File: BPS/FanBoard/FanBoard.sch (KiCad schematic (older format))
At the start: 13 parts, among them J1 Conn_01x02, J2 Conn_01x02, J3 Conn_01x02, J4 Conn_01x02, J5 Conn_01x06, Q1 BUK9M34-100EX, Q2 BUK9M34-100EX, Q3 BUK9M34-100EX, Q4 BUK9M34-100EX

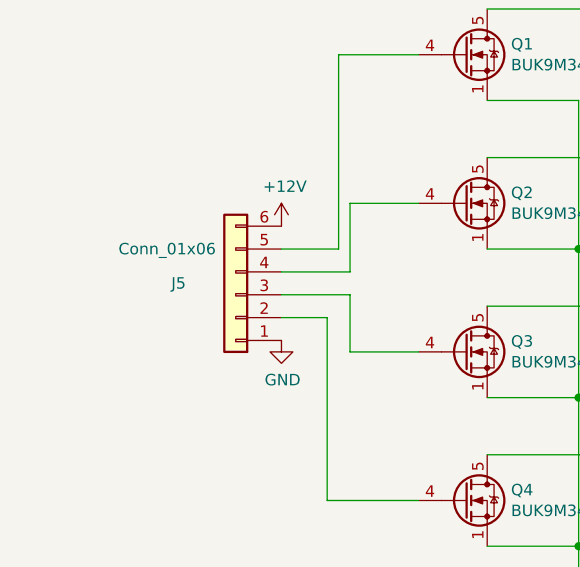
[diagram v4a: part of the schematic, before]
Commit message: Changed Leader board connections and changed footprints of fan connections to molex 3mm
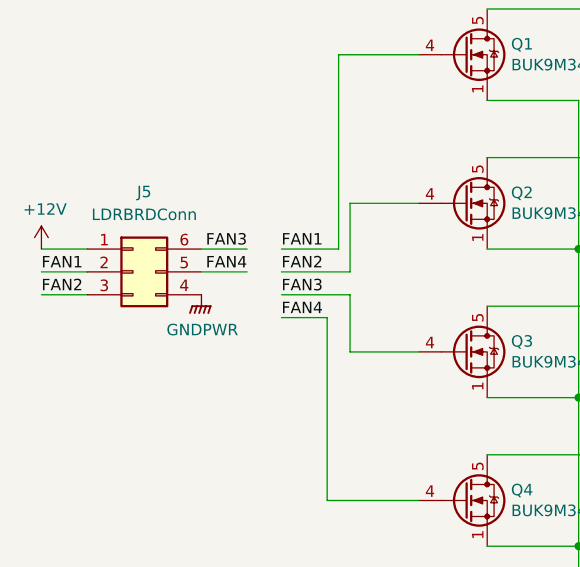
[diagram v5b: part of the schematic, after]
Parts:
- removed J5: Conn_01x06, symbol Connector_Generic:Conn_01x06
- added J5: LDRBRDConn, symbol Connector_Generic:Conn_02x03_Counter_Clockwise
- J1, J2, J3, J4: footprint Connector_PinSocket_2.54mm:PinSocket_1x02_P2.54mm_Vertical -> UTSVT_Connectors:Molex_MicroFit3.0_1x2xP3.00mm_PolarizingPeg_Vertical
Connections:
- net +12V: now also J5.1 (Pin_1)
- net FAN1: now reaches Q1.4 (G)
- net FAN1: now also J5.2 (Pin_2)
- net FAN2: now reaches Q2.4 (G)
- net FAN2: now also J5.3 (Pin_3)
- net FAN3: now reaches Q3.4 (G)
- net FAN3: now also J5.6 (Pin_6)
- net FAN4: now reaches Q4.4 (G)
- net FAN4: now also J5.5 (Pin_5)
- new net GNDPWR: J5.4 (Pin_4)
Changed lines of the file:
@@
 F 0 "J1" H 4330 3642 50  0000 L CNN
 F 1 "Conn_01x02" H 4330 3551 50  0000 L CNN
-F 2 "Connector_PinSocket_2.54mm:PinSocket_1x02_P2.54mm_Vertical" H 4250 3650 50  0001 C CNN
+F 2 "UTSVT_Connectors:Molex_MicroFit3.0_1x2xP3.00mm_PolarizingPeg_Vertical" H 4250 3650 50  0001 C CNN
 F 3 "~" H 4250 3650 50  0001 C CNN
 	1    4250 3650
@@
 F 0 "J2" H 4330 4292 50  0000 L CNN
 F 1 "Conn_01x02" H 4330 4201 50  0000 L CNN
-F 2 "Connector_PinSocket_2.54mm:PinSocket_1x02_P2.54mm_Vertical" H 4250 4300 50  0001 C CNN
+F 2 "UTSVT_Connectors:Molex_MicroFit3.0_1x2xP3.00mm_PolarizingPeg_Vertical" H 4250 4300 50  0001 C CNN
 F 3 "~" H 4250 4300 50  0001 C CNN
 	1    4250 4300
@@
 F 0 "J3" H 4330 4942 50  0000 L CNN
 F 1 "Conn_01x02" H 4330 4851 50  0000 L CNN
-F 2 "Connector_PinSocket_2.54mm:PinSocket_1x02_P2.54mm_Vertical" H 4250 4950 50  0001 C CNN
+F 2 "UTSVT_Connectors:Molex_MicroFit3.0_1x2xP3.00mm_PolarizingPeg_Vertical" H 4250 4950 50  0001 C CNN
 F 3 "~" H 4250 4950 50  0001 C CNN
 	1    4250 4950
@@
 F 0 "J4" H 4330 5592 50  0000 L CNN
 F 1 "Conn_01x02" H 4330 5501 50  0000 L CNN
-F 2 "Connector_PinSocket_2.54mm:PinSocket_1x02_P2.54mm_Vertical" H 4250 5600 50  0001 C CNN
+F 2 "UTSVT_Connectors:Molex_MicroFit3.0_1x2xP3.00mm_PolarizingPeg_Vertical" H 4250 5600 50  0001 C CNN
 F 3 "~" H 4250 5600 50  0001 C CNN
 	1    4250 5600
@@
 	2500 5100 2300 5100
 $Comp
-L Connector_Generic:Conn_01x06 J5
-U 1 1 5F1BB034
-P 2100 5000
-F 0 "J5" H 2350 4950 50  0000 C CNN
-F 1 "Conn_01x06" H 2400 4800 50  0000 C CNN
-F 2 "" H 2100 5000 50  0001 C CNN
-F 3 "~" H 2100 5000 50  0001 C CNN
-	1    2100 5000
-	-1   0    0    1
-$EndComp
-$Comp
 L power:+12V #PWR03
 U 1 1 5F1BC556
-P 2300 4700
-F 0 "#PWR03" H 2300 4550 50  0001 C CNN
-F 1 "+12V" H 2315 4873 50  0000 C CNN
-F 2 "" H 2300 4700 50  0001 C CNN
-F 3 "" H 2300 4700 50  0001 C CNN
-	1    2300 4700
-	1    0    0    -1
-$EndComp
-$Comp
-L power:GND #PWR04
-U 1 1 5F1BCBA1
-P 2300 5200
-F 0 "#PWR04" H 2300 4950 50  0001 C CNN
-F 1 "GND" H 2305 5027 50  0000 C CNN
-F 2 "" H 2300 5200 50  0001 C CNN
-F 3 "" H 2300 5200 50  0001 C CNN
-	1    2300 5200
-	1    0    0    -1
-$EndComp
+P 1250 4800
+F 0 "#PWR03" H 1250 4650 50  0001 C CNN
+F 1 "+12V" H 1265 4973 50  0000 C CNN
+F 2 "" H 1250 4800 50  0001 C CNN
+F 3 "" H 1250 4800 50  0001 C CNN
+	1    1250 4800
+	1    0    0    -1
+$EndComp
+$Comp
+L Connector_Generic:Conn_02x03_Counter_Clockwise J5
+U 1 1 5F1BA642
+P 1650 4900
+F 0 "J5" H 1700 5250 50  0000 C CNN
+F 1 "LDRBRDConn" H 1700 5150 50  0000 C CNN
+F 2 "" H 1650 4900 50  0001 C CNN
+F 3 "~" H 1650 4900 50  0001 C CNN
+	1    1650 4900
+	1    0    0    -1
+$EndComp
+$Comp
+L power:GNDPWR #PWR04
+U 1 1 5F1BB28B
+P 1950 5000
+F 0 "#PWR04" H 1950 4800 50  0001 C CNN
+F 1 "GNDPWR" H 1954 4846 50  0000 C CNN
+F 2 "" H 1950 4950 50  0001 C CNN
+F 3 "" H 1950 4950 50  0001 C CNN
+	1    1950 5000
+	1    0    0    -1
+$EndComp
+Text Label 2300 4800 0    50   ~ 0
+FAN1
+Text Label 2300 4900 0    50   ~ 0
+FAN2
+Text Label 2300 5000 0    50   ~ 0
+FAN3
+Text Label 2300 5100 0    50   ~ 0
+FAN4
+Text Label 1250 4900 0    50   ~ 0
+FAN1
+Text Label 1250 5000 0    50   ~ 0
+FAN2
+Text Label 2150 4800 2    50   ~ 0
+FAN3
+Text Label 2150 4900 2    50   ~ 0
+FAN4
+Wire Wire Line
+	1450 4900 1250 4900
+Wire Wire Line
+	1450 5000 1250 5000
+Wire Wire Line
+	1950 4800 2150 4800
+Wire Wire Line
+	1950 4900 2150 4900
+Wire Wire Line
+	1250 4800 1450 4800
 $EndSCHEMATC

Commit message: Aesthetic changes
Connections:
- net GND is gone; now on net GNDPWR: Q1.1 (S), Q1.2 (S), Q1.3 (S), Q2.1 (S), Q2.2 (S), Q2.3 (S), Q3.1 (S), Q3.2 (S), Q3.3 (S), Q4.1 (S), Q4.2 (S), Q4.3 (S)
- net FAN3: now also J5.5 (Pin_5); no longer J5.6 (Pin_6)
- net FAN4: now also J5.4 (Pin_4); no longer J5.5 (Pin_5)
- net GNDPWR: now also J5.6 (Pin_6); no longer J5.4 (Pin_4)
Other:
- moved on the sheet: J5
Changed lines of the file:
@@
 Wire Wire Line
 	3600 4800 3600 5450
-$Comp
-L power:GND #PWR02
-U 1 1 5F0B61B4
-P 3600 6200
-F 0 "#PWR02" H 3600 5950 50  0001 C CNN
-F 1 "GND" H 3605 6027 50  0000 C CNN
-F 2 "" H 3600 6200 50  0001 C CNN
-F 3 "" H 3600 6200 50  0001 C CNN
-	1    3600 6200
-	1    0    0    -1
-$EndComp
 Wire Wire Line
 	3600 6100 3600 6200
@@
 L power:+12V #PWR03
 U 1 1 5F1BC556
-P 1250 4800
-F 0 "#PWR03" H 1250 4650 50  0001 C CNN
-F 1 "+12V" H 1265 4973 50  0000 C CNN
-F 2 "" H 1250 4800 50  0001 C CNN
-F 3 "" H 1250 4800 50  0001 C CNN
-	1    1250 4800
+P 850 4750
+F 0 "#PWR03" H 850 4600 50  0001 C CNN
+F 1 "+12V" H 865 4923 50  0000 C CNN
+F 2 "" H 850 4750 50  0001 C CNN
+F 3 "" H 850 4750 50  0001 C CNN
+	1    850  4750
 	1    0    0    -1
 $EndComp
@@
 L Connector_Generic:Conn_02x03_Counter_Clockwise J5
 U 1 1 5F1BA642
-P 1650 4900
-F 0 "J5" H 1700 5250 50  0000 C CNN
-F 1 "LDRBRDConn" H 1700 5150 50  0000 C CNN
-F 2 "" H 1650 4900 50  0001 C CNN
-F 3 "~" H 1650 4900 50  0001 C CNN
-	1    1650 4900
+P 1300 4850
+F 0 "J5" H 1350 5200 50  0000 C CNN
+F 1 "LDRBRDConn" H 1350 5100 50  0000 C CNN
+F 2 "" H 1300 4850 50  0001 C CNN
+F 3 "~" H 1300 4850 50  0001 C CNN
+	1    1300 4850
 	1    0    0    -1
 $EndComp
@@
 L power:GNDPWR #PWR04
 U 1 1 5F1BB28B
-P 1950 5000
-F 0 "#PWR04" H 1950 4800 50  0001 C CNN
-F 1 "GNDPWR" H 1954 4846 50  0000 C CNN
-F 2 "" H 1950 4950 50  0001 C CNN
-F 3 "" H 1950 4950 50  0001 C CNN
-	1    1950 5000
+P 1650 5050
+F 0 "#PWR04" H 1650 4850 50  0001 C CNN
+F 1 "GNDPWR" H 1654 4896 50  0000 C CNN
+F 2 "" H 1650 5000 50  0001 C CNN
+F 3 "" H 1650 5000 50  0001 C CNN
+	1    1650 5050
 	1    0    0    -1
 $EndComp
@@
 Text Label 2300 5100 0    50   ~ 0
 FAN4
-Text Label 1250 4900 0    50   ~ 0
+Text Label 850  4850 0    50   ~ 0
 FAN1
-Text Label 1250 5000 0    50   ~ 0
+Text Label 850  4950 0    50   ~ 0
 FAN2
-Text Label 2150 4800 2    50   ~ 0
+Text Label 1850 4850 2    50   ~ 0
 FAN3
-Text Label 2150 4900 2    50   ~ 0
+Text Label 1850 4950 2    50   ~ 0
 FAN4
 Wire Wire Line
-	1450 4900 1250 4900
-Wire Wire Line
-	1450 5000 1250 5000
-Wire Wire Line
-	1950 4800 2150 4800
-Wire Wire Line
-	1950 4900 2150 4900
-Wire Wire Line
-	1250 4800 1450 4800
+	850  4850 1100 4850
+Wire Wire Line
+	850  4950 1100 4950
+Wire Wire Line
+	1600 4850 1850 4850
+Wire Wire Line
+	1600 4950 1850 4950
+Wire Wire Line
+	1600 4750 1650 4750
+Wire Wire Line
+	1650 4750 1650 5050
+$Comp
+L power:GNDPWR #PWR0101
+U 1 1 5F1D2CFD
+P 3600 6200
+F 0 "#PWR0101" H 3600 6000 50  0001 C CNN
+F 1 "GNDPWR" H 3604 6046 50  0000 C CNN
+F 2 "" H 3600 6150 50  0001 C CNN
+F 3 "" H 3600 6150 50  0001 C CNN
+	1    3600 6200
+	1    0    0    -1
+$EndComp
+Wire Wire Line
+	850  4750 1100 4750
 $EndSCHEMATC

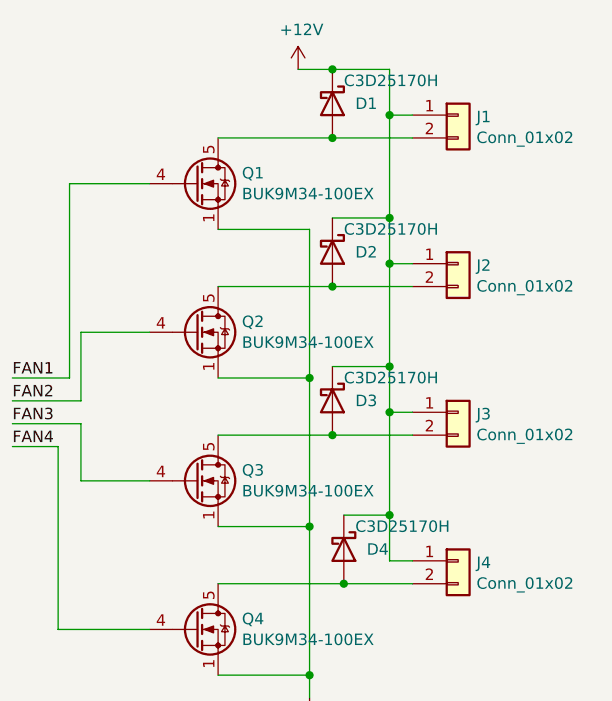
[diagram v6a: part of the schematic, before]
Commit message: Changed diodes used to cheaper ones
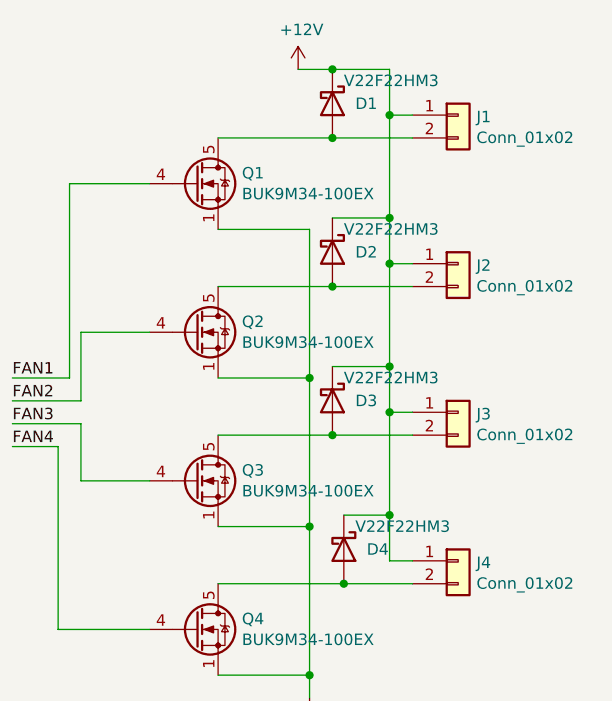
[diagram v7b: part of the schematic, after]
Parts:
- D1, D2, D3, D4: value C3D25170H -> V22F22HM3; footprint Package_TO_SOT_THT:TO-247-2_Vertical -> UTSVT_BPS:V2F22HM
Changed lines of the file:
@@
-$EndComp
-Wire Wire Line
-	3200 4400 3700 4400
-Wire Wire Line
-	3200 5050 3700 5050
-Wire Wire Line
-	3200 3750 3700 3750
-$Comp
-L Transistor_FET:BUK9M34-100EX Q1
-U 1 1 5F0AEA0D
-P 3100 3950
-F 0 "Q1" H 3304 3996 50  0000 L CNN
-F 1 "BUK9M34-100EX" H 3304 3905 50  0000 L CNN
-F 2 "Package_TO_SOT_SMD:LFPAK33" H 3300 3875 50  0001 L CIN
-F 3 "https://assets.nexperia.com/documents/data-sheet/BUK9M34-100E.pdf" V 3100 3950 50  0001 L CNN
-	1    3100 3950
-	1    0    0    -1
-$EndComp
-$Comp
-L Transistor_FET:BUK9M34-100EX Q2
-U 1 1 5F0B1145
-P 3100 4600
-F 0 "Q2" H 3304 4646 50  0000 L CNN
-F 1 "BUK9M34-100EX" H 3304 4555 50  0000 L CNN
-F 2 "Package_TO_SOT_SMD:LFPAK33" H 3300 4525 50  0001 L CIN
-F 3 "https://assets.nexperia.com/documents/data-sheet/BUK9M34-100E.pdf" V 3100 4600 50  0001 L CNN
-	1    3100 4600
-	1    0    0    -1
-$EndComp
-$Comp
-L Transistor_FET:BUK9M34-100EX Q3
-U 1 1 5F0B279A
-P 3100 5250
-F 0 "Q3" H 3304 5296 50  0000 L CNN
-F 1 "BUK9M34-100EX" H 3304 5205 50  0000 L CNN
-F 2 "Package_TO_SOT_SMD:LFPAK33" H 3300 5175 50  0001 L CIN
-F 3 "https://assets.nexperia.com/documents/data-sheet/BUK9M34-100E.pdf" V 3100 5250 50  0001 L CNN
-	1    3100 5250
-	1    0    0    -1
-$EndComp
-$Comp
-L Transistor_FET:BUK9M34-100EX Q4
-U 1 1 5F0B2EF7
-P 3100 5900
-F 0 "Q4" H 3304 5946 50  0000 L CNN
-F 1 "BUK9M34-100EX" H 3304 5855 50  0000 L CNN
-F 2 "Package_TO_SOT_SMD:LFPAK33" H 3300 5825 50  0001 L CIN
-F 3 "https://assets.nexperia.com/documents/data-sheet/BUK9M34-100E.pdf" V 3100 5900 50  0001 L CNN
-	1    3100 5900
-	1    0    0    -1
 $EndComp
 Wire Wire Line
@@
 Wire Wire Line
 	3600 6100 3600 6200
-$Comp
-L Diode:C3D25170H D2
-U 1 1 5F0A0D46
-P 3700 4250
-F 0 "D2" V 3700 4350 50  0000 L CNN
-F 1 "C3D25170H" V 3600 4300 50  0000 L CNN
-F 2 "Package_TO_SOT_THT:TO-247-2_Vertical" H 3700 4075 50  0001 C CNN
-F 3 "https://www.wolfspeed.com/media/downloads/103/C3D25170H.pdf" H 3700 4250 50  0001 C CNN
-	1    3700 4250
-	0    1    1    0
-$EndComp
-Wire Wire Line
-	3200 5700 3750 5700
-Connection ~ 3700 4400
-Wire Wire Line
-	3700 4400 4050 4400
-$Comp
-L Diode:C3D25170H D1
-U 1 1 5F0A355E
-P 3700 3600
-F 0 "D1" V 3700 3700 50  0000 L CNN
-F 1 "C3D25170H" V 3600 3650 50  0000 L CNN
-F 2 "Package_TO_SOT_THT:TO-247-2_Vertical" H 3700 3425 50  0001 C CNN
-F 3 "https://www.wolfspeed.com/media/downloads/103/C3D25170H.pdf" H 3700 3600 50  0001 C CNN
-	1    3700 3600
-	0    1    1    0
-$EndComp
-$Comp
-L Diode:C3D25170H D3
-U 1 1 5F0A37E3
-P 3700 4900
-F 0 "D3" V 3700 5000 50  0000 L CNN
-F 1 "C3D25170H" V 3600 4950 50  0000 L CNN
-F 2 "Package_TO_SOT_THT:TO-247-2_Vertical" H 3700 4725 50  0001 C CNN
-F 3 "https://www.wolfspeed.com/media/downloads/103/C3D25170H.pdf" H 3700 4900 50  0001 C CNN
-	1    3700 4900
-	0    1    1    0
-$EndComp
-$Comp
-L Diode:C3D25170H D4
-U 1 1 5F0A3942
-P 3750 5550
-F 0 "D4" V 3750 5650 50  0000 L CNN
-F 1 "C3D25170H" V 3650 5600 50  0000 L CNN
-F 2 "Package_TO_SOT_THT:TO-247-2_Vertical" H 3750 5375 50  0001 C CNN
-F 3 "https://www.wolfspeed.com/media/downloads/103/C3D25170H.pdf" H 3750 5550 50  0001 C CNN
-	1    3750 5550
-	0    1    1    0
-$EndComp
 Wire Wire Line
 	4050 5600 3950 5600
 Wire Wire Line
 	3950 5600 3950 5400
-Wire Wire Line
-	3950 3450 3700 3450
-Connection ~ 3700 3450
-Wire Wire Line
-	3700 3450 3550 3450
 Wire Wire Line
 	4050 3650 3950 3650
@@
 Wire Wire Line
 	3950 5400 3950 4950
-Connection ~ 3700 3750
-Wire Wire Line
-	3700 3750 4050 3750
-Connection ~ 3700 5050
-Wire Wire Line
-	3700 5050 4050 5050
-Connection ~ 3750 5700
-Wire Wire Line
-	3750 5700 4050 5700
 Wire Wire Line
 	2900 3950 2550 3950
@@
 Wire Wire Line
 	850  4750 1100 4750
+$Comp
+L Transistor_FET:BUK9M34-100EX Q4
+U 1 1 5F0B2EF7
+P 3100 5900
+F 0 "Q4" H 3304 5946 50  0000 L CNN
+F 1 "BUK9M34-100EX" H 3304 5855 50  0000 L CNN
+F 2 "Package_TO_SOT_SMD:LFPAK33" H 3300 5825 50  0001 L CIN
+F 3 "https://assets.nexperia.com/documents/data-sheet/BUK9M34-100E.pdf" V 3100 5900 50  0001 L CNN
+	1    3100 5900
+	1    0    0    -1
+$EndComp
+$Comp
+L Transistor_FET:BUK9M34-100EX Q3
+U 1 1 5F0B279A
+P 3100 5250
+F 0 "Q3" H 3304 5296 50  0000 L CNN
+F 1 "BUK9M34-100EX" H 3304 5205 50  0000 L CNN
+F 2 "Package_TO_SOT_SMD:LFPAK33" H 3300 5175 50  0001 L CIN
+F 3 "https://assets.nexperia.com/documents/data-sheet/BUK9M34-100E.pdf" V 3100 5250 50  0001 L CNN
+	1    3100 5250
+	1    0    0    -1
+$EndComp
+$Comp
+L Transistor_FET:BUK9M34-100EX Q2
+U 1 1 5F0B1145
+P 3100 4600
+F 0 "Q2" H 3304 4646 50  0000 L CNN
+F 1 "BUK9M34-100EX" H 3304 4555 50  0000 L CNN
+F 2 "Package_TO_SOT_SMD:LFPAK33" H 3300 4525 50  0001 L CIN
+F 3 "https://assets.nexperia.com/documents/data-sheet/BUK9M34-100E.pdf" V 3100 4600 50  0001 L CNN
+	1    3100 4600
+	1    0    0    -1
+$EndComp
+$Comp
+L Transistor_FET:BUK9M34-100EX Q1
+U 1 1 5F0AEA0D
+P 3100 3950
+F 0 "Q1" H 3304 3996 50  0000 L CNN
+F 1 "BUK9M34-100EX" H 3304 3905 50  0000 L CNN
+F 2 "Package_TO_SOT_SMD:LFPAK33" H 3300 3875 50  0001 L CIN
+F 3 "https://assets.nexperia.com/documents/data-sheet/BUK9M34-100E.pdf" V 3100 3950 50  0001 L CNN
+	1    3100 3950
+	1    0    0    -1
+$EndComp
+Wire Wire Line
+	3750 5700 4050 5700
+Wire Wire Line
+	3200 5700 3750 5700
+Connection ~ 3750 5700
+$Comp
+L Diode:C3D25170H D4
+U 1 1 5F0A3942
+P 3750 5550
+F 0 "D4" V 3750 5650 50  0000 L CNN
+F 1 "V22F22HM3" V 3650 5600 50  0000 L CNN
+F 2 "UTSVT_BPS:V2F22HM" H 3750 5375 50  0001 C CNN
+F 3 "https://www.wolfspeed.com/media/downloads/103/C3D25170H.pdf" H 3750 5550 50  0001 C CNN
+	1    3750 5550
+	0    1    1    0
+$EndComp
+Wire Wire Line
+	3700 5050 4050 5050
+Wire Wire Line
+	3200 5050 3700 5050
+Connection ~ 3700 5050
+$Comp
+L Diode:C3D25170H D3
+U 1 1 5F0A37E3
+P 3700 4900
+F 0 "D3" V 3700 5000 50  0000 L CNN
+F 1 "V22F22HM3" V 3600 4950 50  0000 L CNN
+F 2 "UTSVT_BPS:V2F22HM" H 3700 4725 50  0001 C CNN
+F 3 "https://www.wolfspeed.com/media/downloads/103/C3D25170H.pdf" H 3700 4900 50  0001 C CNN
+	1    3700 4900
+	0    1    1    0
+$EndComp
+Wire Wire Line
+	3700 4400 4050 4400
+Wire Wire Line
+	3200 4400 3700 4400
+Connection ~ 3700 4400
+$Comp
+L Diode:C3D25170H D2
+U 1 1 5F0A0D46
+P 3700 4250
+F 0 "D2" V 3700 4350 50  0000 L CNN
+F 1 "V22F22HM3" V 3600 4300 50  0000 L CNN
+F 2 "UTSVT_BPS:V2F22HM" H 3700 4075 50  0001 C CNN
+F 3 "https://www.wolfspeed.com/media/downloads/103/C3D25170H.pdf" H 3700 4250 50  0001 C CNN
+	1    3700 4250
+	0    1    1    0
+$EndComp
+Wire Wire Line
+	3700 3750 4050 3750
+Wire Wire Line
+	3200 3750 3700 3750
+Connection ~ 3700 3750
+Wire Wire Line
+	3700 3450 3550 3450
+Wire Wire Line
+	3950 3450 3700 3450
+Connection ~ 3700 3450
+$Comp
+L Diode:C3D25170H D1
+U 1 1 5F0A355E
+P 3700 3600
+F 0 "D1" V 3700 3700 50  0000 L CNN
+F 1 "V22F22HM3" V 3600 3650 50  0000 L CNN
+F 2 "UTSVT_BPS:V2F22HM" H 3700 3425 50  0001 C CNN
+F 3 "https://www.wolfspeed.com/media/downloads/103/C3D25170H.pdf" H 3700 3600 50  0001 C CNN
+	1    3700 3600
+	0    1    1    0
+$EndComp
 $EndSCHEMATC

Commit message: Finished Fan Board PCB
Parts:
- J5: footprint (none) -> Connector_Molex:Molex_Micro-Fit_3.0_43045-0612_2x03_P3.00mm_Vertical
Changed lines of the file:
@@
 F 0 "J5" H 1350 5200 50  0000 C CNN
 F 1 "LDRBRDConn" H 1350 5100 50  0000 C CNN
-F 2 "" H 1300 4850 50  0001 C CNN
+F 2 "Connector_Molex:Molex_Micro-Fit_3.0_43045-0612_2x03_P3.00mm_Vertical" H 1300 4850 50  0001 C CNN
 F 3 "~" H 1300 4850 50  0001 C CNN
 	1    1300 4850
